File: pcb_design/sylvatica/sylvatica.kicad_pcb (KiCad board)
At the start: 2 copper layers, 93 x 93 mm, 121 parts, among them J1 USB_C_Receptacle, J2 USB_C_Receptacle, J3 USB_C_Receptacle, J4 USB_C_Receptacle, J5 Conn_02x07_Odd_Even, J6 Conn_02x07_Odd_Even, J9 Conn_01x06_Female, Q1 Q_NMOS_GSD, Q2 Q_NMOS_GSD, SW1 SW_Push, U1 PGA113, U10 dsPIC33EP512MC806, U11 SiP32431, U12 LP2985-5.0, U13 REF2033, U14 OPA320, U15 SiP32431, U16 SiP32431, U17 SiP32431, U18 SiP32431, U19 ADM7170, U2 PGA113, U20 MCP2542FD, U21 TPS737, U22 SiP32431, U3 PGA113, U4 PGA113, U5 PGA113, U6 PGA113, U7 PGA113, U8 PGA113, U9 ADS8332, Y1 Crystal_GND24

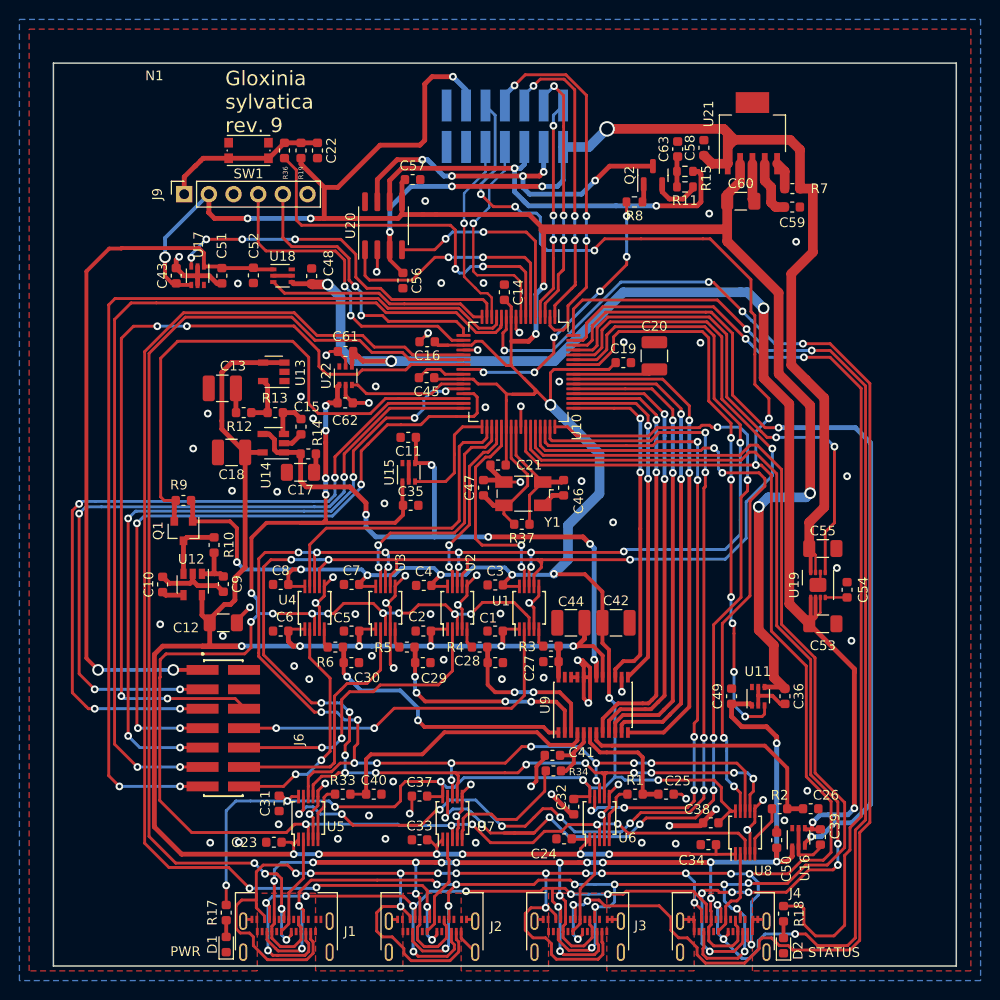
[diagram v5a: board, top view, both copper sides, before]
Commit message: Minor improvements.
Mostly related to external pull-ups of 10k for I2C
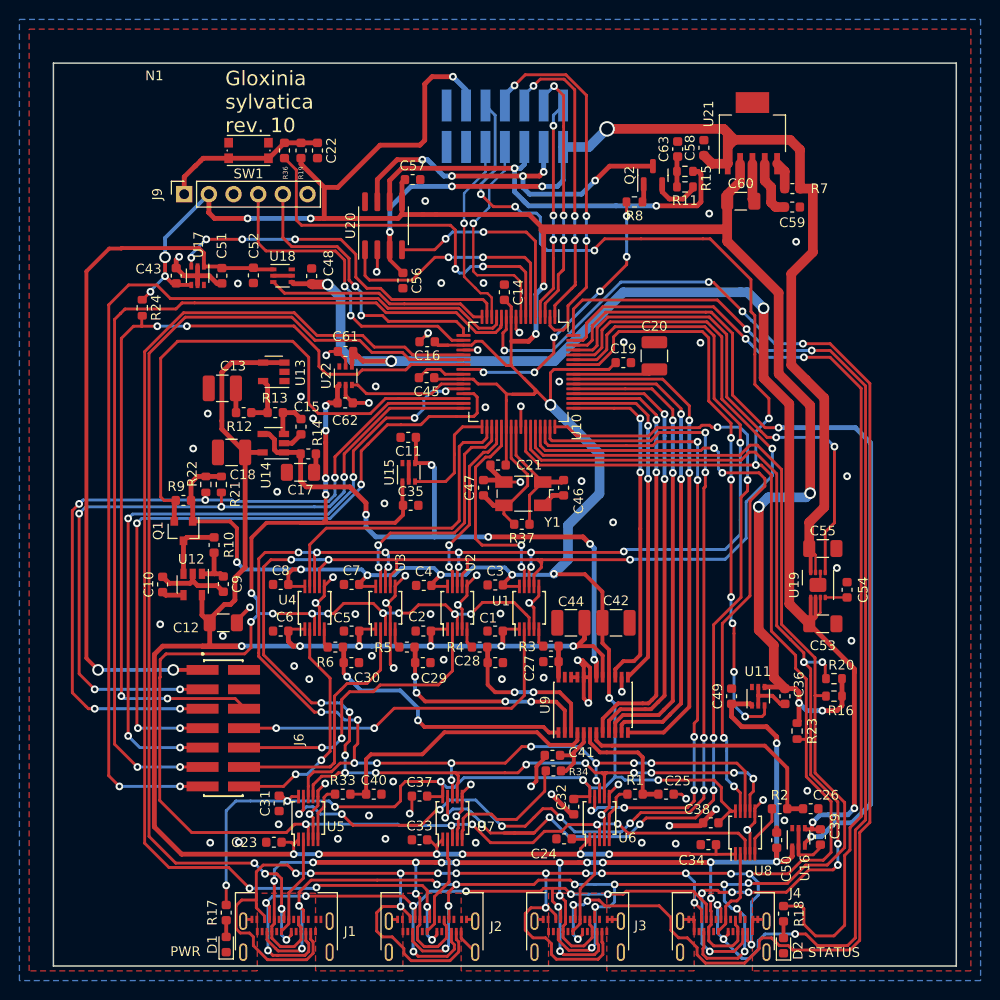
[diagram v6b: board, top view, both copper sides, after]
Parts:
- added R16: 10k, Resistor_SMD:R_0603_1608Metric, F.Cu at (118.9, 103.7)
- added R20: 10k, Resistor_SMD:R_0603_1608Metric, F.Cu at (118.9, 101.9)
- added R21: 10k, Resistor_SMD:R_0603_1608Metric, F.Cu at (55.8, 81.9)
- added R22: 10k, Resistor_SMD:R_0603_1608Metric, F.Cu at (54.2, 81.9)
- added R23: 10k, Resistor_SMD:R_0603_1608Metric, F.Cu at (115.1, 107.3)
- added R24: 10k, Resistor_SMD:R_0603_1608Metric, F.Cu at (47.6, 63.7)
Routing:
- net +3.3V: track 431.1 -> 452.4 mm, vias 22 -> 26
- net /SDA1: track 189.8 -> 193.6 mm, vias 16 -> 18
- net /SCL2: track 76.4 -> 77.9 mm, vias 4 -> 5
- net /OW8: track 101.2 -> 102.3 mm
- net /SCL1: track 186.7 -> 187.9 mm
- net /~{INT2}: track 89.3 -> 90.4 mm
- net /~{INT1}: track 277.2 -> 278.2 mm
- net /SDA2: track 80.2 -> 81.1 mm, vias 4 -> 5
- net GND: vias 81 -> 80
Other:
- board text added: "Gloxinia sylvatica rev. 10"
- board text removed: "Gloxinia sylvatica rev. 9"
